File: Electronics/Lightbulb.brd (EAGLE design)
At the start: 61 x 47 mm, 19 parts, among them IC2 7805L

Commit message: correct spacing on pushbuttons
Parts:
- moved U$1 2.38 mm to (6.50, 17.1)
- moved U$2 0.87 mm to (6.50, 9.07)
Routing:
- net N$4: track 60.2 -> 59.3 mm, vias 1 -> 0
- net VCC: track 49.3 -> 48.6 mm
- net N$6: track 73.6 -> 74.2 mm
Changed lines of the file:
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@@
 <setting verticaltext="up"/>
 </settings>
-<grid distance="1" unitdist="mm" unit="mm" style="lines" multiple="1" display="yes" altdistance="0.1" altunitdist="mm" altunit="mm"/>
+<grid distance="0.1" unitdist="mm" unit="mm" style="lines" multiple="1" display="yes" altdistance="0.1" altunitdist="mm" altunit="mm"/>
 <layers>
 <layer number="1" name="Top" color="4" fill="1" visible="yes" active="yes"/>
@@
 <attribute name="VALUE" x="21.075" y="32.126" size="1.27" layer="28" ratio="10" rot="MR0"/>
 </element>
-<element name="U$2" library="Custom Library" package="SKRPABE010" value="SKRPABE010" x="6.1" y="8.3" rot="MR0"/>
-<element name="U$1" library="Custom Library" package="SKRPABE010" value="SKRPABE010" x="7.9" y="19" rot="MR0"/>
+<element name="U$2" library="Custom Library" package="SKRPABE010" value="SKRPABE010" x="6.5" y="9.075" rot="MR0"/>
+<element name="U$1" library="Custom Library" package="SKRPABE010" value="SKRPABE010" x="6.5" y="17.075" rot="MR0"/>
 </elements>
 <signals>
@@
 <contactref element="U$2" pad="1"/>
 <contactref element="U$2" pad="2"/>
-<wire x1="6.1" y1="10.45" x2="1.95" y2="10.45" width="0.3048" layer="16"/>
-<wire x1="1.1684" y1="11.2316" x2="1.95" y2="10.45" width="0.3048" layer="16"/>
+<wire x1="6.5" y1="11.225" x2="2.35" y2="11.225" width="0.3048" layer="16"/>
 <wire x1="6" y1="30" x2="1.1684" y2="25.1684" width="0.3048" layer="16"/>
-<wire x1="1.1684" y1="25.1684" x2="1.1684" y2="11.2316" width="0.3048" layer="16"/>
+<wire x1="1.1684" y1="25.1684" x2="1.1684" y2="12.4066" width="0.3048" layer="16"/>
+<wire x1="1.1684" y1="12.4066" x2="2.35" y2="11.225" width="0.3048" layer="16"/>
 </signal>
 <signal name="N$8">
@@
 <wire x1="8.8316" y1="1.1684" x2="7" y2="3" width="0.3048" layer="1"/>
 <via x="7" y="3" extent="1-16" drill="0.508"/>
-<wire x1="7" y1="3" x2="7" y2="7.4" width="0.3048" layer="16"/>
-<wire x1="7" y1="7.4" x2="6.1" y2="8.3" width="0.3048" layer="16"/>
-<wire x1="6.1" y1="8.3" x2="1.95" y2="8.3" width="0.3048" layer="16"/>
+<wire x1="6.5" y1="9.075" x2="2.35" y2="9.075" width="0.3048" layer="16"/>
+<wire x1="7" y1="3" x2="7" y2="8.575" width="0.3048" layer="16"/>
+<wire x1="7" y1="8.575" x2="6.5" y2="9.075" width="0.3048" layer="16"/>
 </signal>
 <signal name="N$4">
@@
 <contactref element="C3" pad="1"/>
 <contactref element="IC2" pad="1"/>
-<wire x1="12.2" y1="28.8" x2="6.8" y2="28.8" width="0.3048" layer="1"/>
-<wire x1="6.8" y1="28.8" x2="5.965" y2="27.965" width="0.3048" layer="1"/>
 <wire x1="50.72" y1="34.28" x2="48.97" y2="34.23" width="0.3048" layer="1"/>
 <wire x1="48.97" y1="34.23" x2="45.43" y2="34.23" width="0.3048" layer="1"/>
@@
 <wire x1="33" y1="28" x2="15.771975" y2="28" width="0.3048" layer="16"/>
 <wire x1="39.23" y1="34.23" x2="33" y2="28" width="0.3048" layer="16"/>
-<via x="5.965" y="27.965" extent="1-16" drill="0.508"/>
-<wire x1="5.965" y1="27.965" x2="5.965" y2="23.085" width="0.3048" layer="16"/>
-<wire x1="7.9" y1="21.15" x2="5.965" y2="23.085" width="0.3048" layer="16"/>
-<wire x1="7.9" y1="21.15" x2="3.75" y2="21.15" width="0.3048" layer="16"/>
+<wire x1="6.5" y1="19.225" x2="2.35" y2="19.225" width="0.3048" layer="16"/>
+<wire x1="12.2" y1="28.8" x2="10.4" y2="27" width="0.3048" layer="16"/>
+<wire x1="10.4" y1="27" x2="8" y2="27" width="0.3048" layer="16"/>
+<wire x1="8" y1="27" x2="6.5" y2="25.5" width="0.3048" layer="16"/>
+<wire x1="6.5" y1="25.5" x2="6.5" y2="19.225" width="0.3048" layer="16"/>
 </signal>
 <signal name="N$3">
@@
 <wire x1="10.53" y1="20.53" x2="10" y2="20" width="0.3048" layer="1"/>
 <wire x1="10.53" y1="23.28" x2="10.53" y2="20.53" width="0.3048" layer="1"/>
-<wire x1="7.9" y1="19" x2="7.9" y2="18.1" width="0.3048" layer="16"/>
-<wire x1="9" y1="17" x2="7.9" y2="18.1" width="0.3048" layer="16"/>
-<wire x1="7.9" y1="19" x2="3.75" y2="19" width="0.3048" layer="16"/>
+<wire x1="9" y1="17" x2="8.925" y2="17.075" width="0.3048" layer="16"/>
+<wire x1="8.925" y1="17.075" x2="6.5" y2="17.075" width="0.3048" layer="16"/>
+<wire x1="6.5" y1="17.075" x2="2.35" y2="17.075" width="0.3048" layer="16"/>
 </signal>
 </signals>

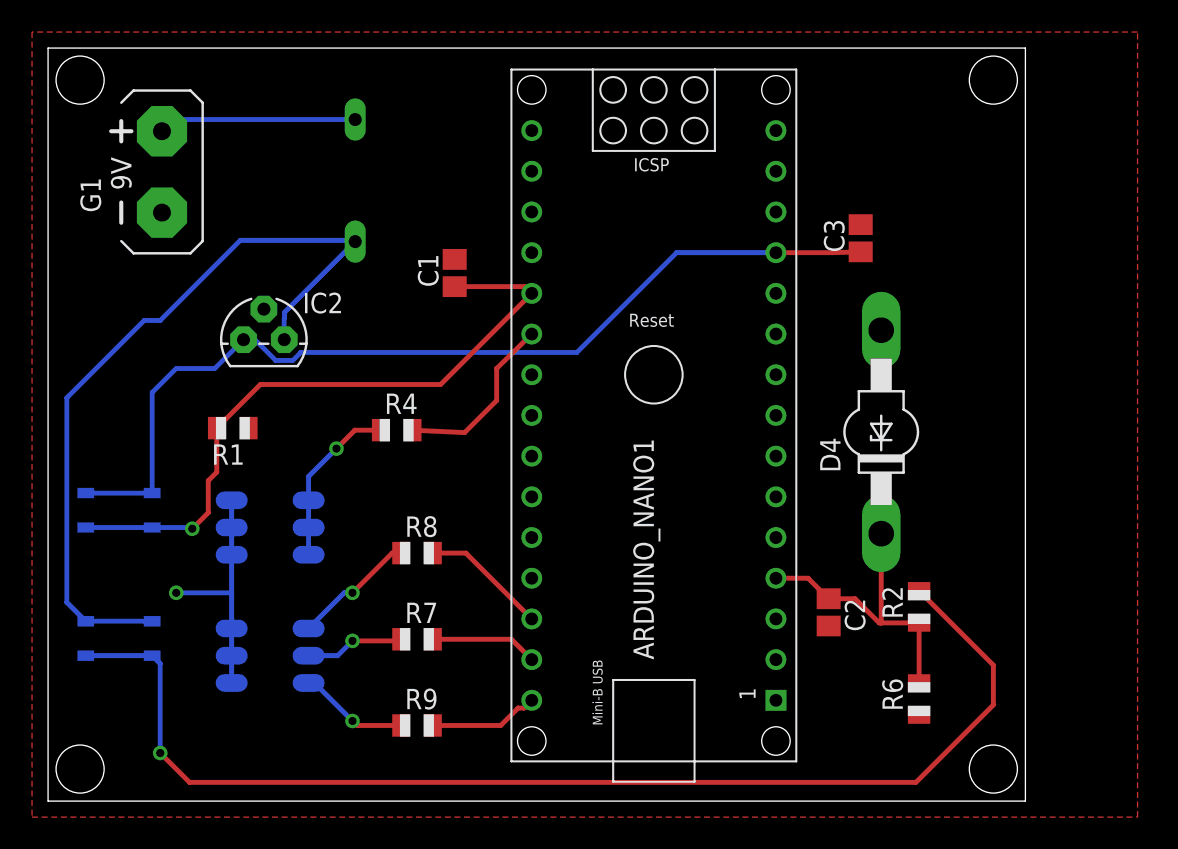
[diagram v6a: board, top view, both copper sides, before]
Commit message: Larger trace widths and new footprint for dip switch
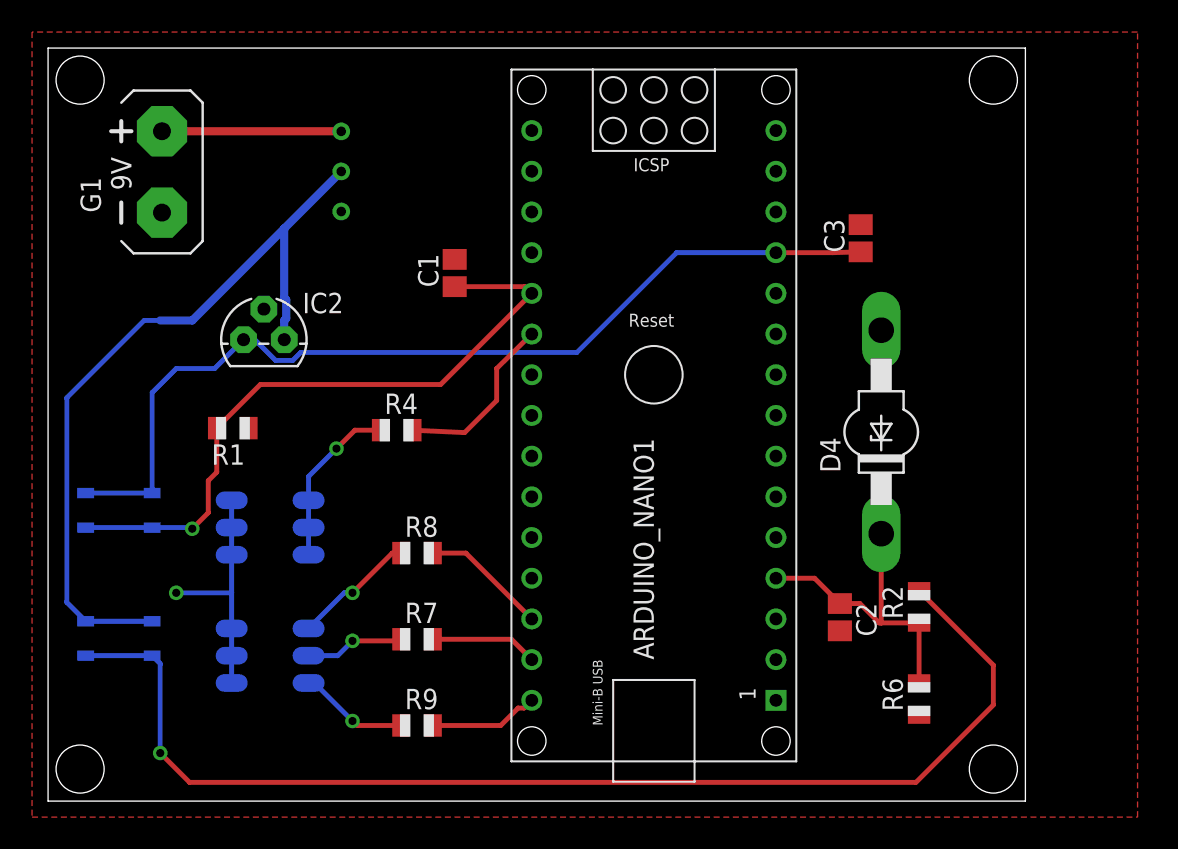
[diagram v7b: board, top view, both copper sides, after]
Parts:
- removed SW1: (no value), special:EDG-01
- added U$3: DIPSWITCH, Custom Library:DIPSWITCH
- moved C2 0.76 mm to (49.4, 11.5)
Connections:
- net GND: now also U$3.P$3
- net N$1: now also U$3.P$1; no longer SW1.2
- net VCC: now also U$3.P$2; no longer SW1.1
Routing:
- net N$1: track 12.4 -> 11.2 mm
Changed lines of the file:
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@@
 </variantdefs>
 <classes>
-<class number="0" name="default" width="0.3048" drill="0.508">
+<class number="0" name="default" width="0.508" drill="0.508">
 <clearance class="0" value="0.3048"/>
 </class>
@@
 <attribute name="VALUE" x="27.666" y="32.071" size="1.27" layer="27" rot="R90"/>
 </element>
-<element name="C2" library="adafruit" package="C0805" value="0.1µF" x="48.72" y="11.78" rot="R270">
-<attribute name="NAME" x="49.736" y="12.669" size="1.27" layer="25" rot="R270"/>
-<attribute name="VALUE" x="46.434" y="12.669" size="1.27" layer="27" rot="R270"/>
+<element name="C2" library="adafruit" package="C0805" value="0.1µF" x="49.42" y="11.48" rot="R270">
+<attribute name="NAME" x="50.436" y="12.369" size="1.27" layer="25" rot="R270"/>
+<attribute name="VALUE" x="47.134" y="12.369" size="1.27" layer="27" rot="R270"/>
 </element>
 <element name="C3" library="adafruit" package="C0805" value="0.1µF" x="50.72" y="35.13" rot="R90">
@@
 <attribute name="VALUE" x="22.268" y="2.434" size="1.27" layer="27"/>
 </element>
-<element name="SW1" library="special" library_urn="urn:adsk.eagle:library:367" package="EDG-01" package3d_urn="urn:adsk.eagle:package:26661/1" value="" x="19.17" y="38.73" rot="MR0">
-<attribute name="NAME" x="21.075" y="44.064" size="1.27" layer="26" ratio="10" rot="MR0"/>
-<attribute name="VALUE" x="21.075" y="32.126" size="1.27" layer="28" ratio="10" rot="MR0"/>
-</element>
 <element name="U$2" library="Custom Library" package="SKRPABE010" value="SKRPABE010" x="6.5" y="9.075" rot="MR0"/>
 <element name="U$1" library="Custom Library" package="SKRPABE010" value="SKRPABE010" x="6.5" y="17.075" rot="MR0"/>
+<element name="U$3" library="Custom Library" package="DIPSWITCH" value="DIPSWITCH" x="18.3" y="41.8" rot="R180"/>
 </elements>
 <signals>
@@
 <wire x1="11.46" y1="13" x2="8" y2="13" width="0.3048" layer="16"/>
 <via x="8" y="13" extent="1-16" drill="0.508"/>
+<contactref element="U$3" pad="P$3"/>
 </signal>
 <signal name="VIN">
@@
 <wire x1="54.365" y1="11.12" x2="52" y2="11.12" width="0.3048" layer="1"/>
 <wire x1="52" y1="11.12" x2="51.88" y2="11.12" width="0.3048" layer="1"/>
-<wire x1="50.37" y1="12.63" x2="48.72" y2="12.63" width="0.3048" layer="1"/>
-<wire x1="51.88" y1="11.12" x2="50.37" y2="12.63" width="0.3048" layer="1"/>
-<wire x1="48.72" y1="12.63" x2="47.44" y2="13.91" width="0.3048" layer="1"/>
-<wire x1="47.44" y1="13.91" x2="45.43" y2="13.91" width="0.3048" layer="1"/>
+<wire x1="50.67" y1="12.33" x2="49.42" y2="12.33" width="0.3048" layer="1"/>
+<wire x1="51.88" y1="11.12" x2="50.67" y2="12.33" width="0.3048" layer="1"/>
+<wire x1="49.42" y1="12.33" x2="47.84" y2="13.91" width="0.3048" layer="1"/>
+<wire x1="47.84" y1="13.91" x2="45.43" y2="13.91" width="0.3048" layer="1"/>
 <wire x1="52" y1="16.69" x2="52" y2="11.12" width="0.3048" layer="1"/>
 </signal>
@@
 <signal name="VCC">
 <contactref element="IC2" pad="3"/>
-<contactref element="SW1" pad="1"/>
-<wire x1="19.17" y1="34.92" x2="14.7654" y2="30.5154" width="0.3048" layer="16"/>
-<wire x1="14.7654" y1="30.5154" x2="14.7654" y2="30.168425" width="0.3048" layer="16"/>
-<wire x1="14.7654" y1="30.168425" x2="14.74" y2="30.143025" width="0.3048" layer="16"/>
-<wire x1="14.74" y1="30.143025" x2="14.74" y2="28.8" width="0.3048" layer="16"/>
-<wire x1="19.17" y1="34.92" x2="19.09" y2="35" width="0.3048" layer="16"/>
 <wire x1="7" y1="30" x2="6" y2="30" width="0.3048" layer="16"/>
-<wire x1="19.09" y1="35" x2="12" y2="35" width="0.3048" layer="16"/>
-<wire x1="12" y1="35" x2="7" y2="30" width="0.3048" layer="16"/>
 <contactref element="U$2" pad="1"/>
 <contactref element="U$2" pad="2"/>
@@
 <wire x1="1.1684" y1="25.1684" x2="1.1684" y2="12.4066" width="0.3048" layer="16"/>
 <wire x1="1.1684" y1="12.4066" x2="2.35" y2="11.225" width="0.3048" layer="16"/>
+<contactref element="U$3" pad="P$2"/>
+<wire x1="18.3" y1="39.3" x2="14.74" y2="35.74" width="0.508" layer="16"/>
+<wire x1="14.74" y1="35.74" x2="14.74" y2="31.4106625" width="0.508" layer="16"/>
+<wire x1="14.74" y1="31.4106625" x2="14.867" y2="31.2836625" width="0.508" layer="16"/>
+<wire x1="14.867" y1="31.2836625" x2="14.867" y2="30.1263375" width="0.508" layer="16"/>
+<wire x1="14.867" y1="30.1263375" x2="14.74" y2="29.9993375" width="0.508" layer="16"/>
+<wire x1="14.74" y1="29.9993375" x2="14.74" y2="28.8" width="0.508" layer="16"/>
+<wire x1="14.74" y1="35.74" x2="9" y2="30" width="0.508" layer="16"/>
+<wire x1="9" y1="30" x2="7" y2="30" width="0.508" layer="16"/>
 </signal>
 <signal name="N$8">
@@
 <wire x1="28.92" y1="10.1" x2="24.03" y2="10.1" width="0.3048" layer="1"/>
 <wire x1="30.19" y1="8.83" x2="28.92" y2="10.1" width="0.3048" layer="1"/>
-</signal>
-<signal name="N$1">
-<contactref element="G1" pad="+"/>
-<contactref element="SW1" pad="2"/>
-<wire x1="19.17" y1="42.54" x2="7.84" y2="42.54" width="0.3048" layer="16"/>
-<wire x1="7.84" y1="42.54" x2="7.11" y2="41.81" width="0.3048" layer="16"/>
 </signal>
 <signal name="N$2">
@@
 <wire x1="6.5" y1="17.075" x2="2.35" y2="17.075" width="0.3048" layer="16"/>
 </signal>
+<signal name="N$1">
+<contactref element="G1" pad="+"/>
+<contactref element="U$3" pad="P$1"/>
+<wire x1="7.11" y1="41.81" x2="18.29" y2="41.81" width="0.508" layer="1"/>
+<wire x1="18.29" y1="41.81" x2="18.3" y2="41.8" width="0.508" layer="1"/>
+</signal>
 </signals>
 <mfgpreviewcolors>
@@
 <mfgpreviewcolor name="substratecolor" color="0xFF786E46"/>
 </mfgpreviewcolors>
+<errors>
+</errors>
 </board>
 </drawing>

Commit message: Correct trace widths this time (Matt Brown approved)
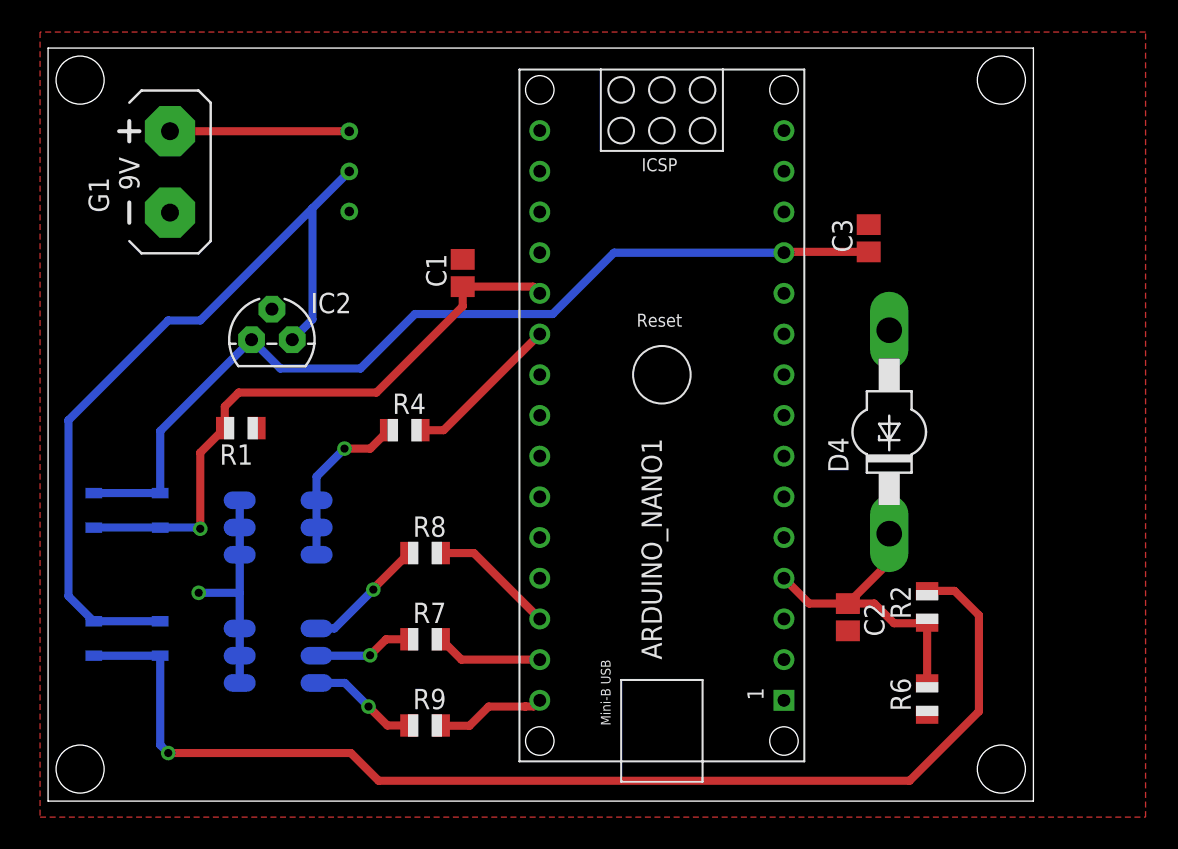
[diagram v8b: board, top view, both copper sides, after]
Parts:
- moved ARDUINO_NANO1 0.50 mm to (38.3, 26.6)
- moved C1 0.50 mm to (25.9, 33.0)
- moved C2 0.50 mm to (49.9, 11.5)
- moved C3 0.50 mm to (51.2, 35.1)
- moved D2 0.50 mm to (14.4, 17.1)
- moved D3 0.50 mm to (14.4, 9.07)
- moved D4 0.50 mm to (52.5, 23.0)
- moved G1 0.50 mm to (7.61, 39.3)
- moved IC2 0.50 mm to (14.0, 28.8)
- moved R1 0.50 mm to (12.0, 23.3)
- moved R2 0.50 mm to (54.9, 12.1)
- moved R4 0.50 mm to (22.3, 23.1)
- moved R6 0.50 mm to (54.9, 6.37)
- moved R7 0.50 mm to (23.5, 10.1)
- moved R8 0.50 mm to (23.5, 15.5)
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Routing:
- net N$3: track 41.7 -> 38.6 mm
- net VCC: track 48.6 -> 50.0 mm
- net N$7: track 11.1 -> 9.92 mm
- net N$4: track 59.3 -> 58.4 mm
- net GND: track 14.9 -> 14.0 mm
- net N$6: track 74.2 -> 73.4 mm
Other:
- board size 61 x 47 mm -> 61.5 x 47 mm
